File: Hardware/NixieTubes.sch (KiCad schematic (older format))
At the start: 14 parts, among them U1 HV5623K7-G, U2 HV5623K7-G

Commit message: Start rework
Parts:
- N1, N2, N3, N4: footprint Nixies:nixies-us-IN-14 -> Nixies:IN-14
- U1, U2: value HV5623K7-G -> HV5530; footprint hv5623:HV5623K7-G -> Package_QFP:PQFP-44_10x10mm_P0.8mm; symbol 2020-07-19_08-41-54:HV5623K7-G -> HV_Shift_Register:HV5530
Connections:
- wire segments 135 -> 131
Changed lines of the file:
@@
 Wire Wire Line
 	950  3300 1150 3300
-Text GLabel 3500 4100 2    50   Input ~ 0
+Text GLabel 3500 4000 2    50   Input ~ 0
 NIX_LE
-Text GLabel 3500 4000 2    50   Input ~ 0
+Text GLabel 3500 3900 2    50   Input ~ 0
 NIX_DATA
-Text GLabel 3500 4400 2    50   Input ~ 0
+Text GLabel 3500 4300 2    50   Input ~ 0
 NIX_CLK
 Wire Wire Line
-	3350 4400 3500 4400
-Wire Wire Line
-	3350 4100 3500 4100
+	3350 4300 3500 4300
 Wire Wire Line
 	3350 4000 3500 4000
+Wire Wire Line
+	3350 3900 3500 3900
 $Comp
 L power:+5V #PWR0101
 U 1 1 5F1E1656
-P 3500 4200
-F 0 "#PWR0101" H 3500 4050 50  0001 C CNN
-F 1 "+5V" V 3515 4328 50  0000 L CNN
-F 2 "" H 3500 4200 50  0001 C CNN
-F 3 "" H 3500 4200 50  0001 C CNN
-	1    3500 4200
+P 3500 4100
+F 0 "#PWR0101" H 3500 3950 50  0001 C CNN
+F 1 "+5V" V 3515 4228 50  0000 L CNN
+F 2 "" H 3500 4100 50  0001 C CNN
+F 3 "" H 3500 4100 50  0001 C CNN
+	1    3500 4100
 	0    1    1    0
 $EndComp
-Wire Wire Line
-	3500 4200 3350 4200
 $Comp
 L power:+5V #PWR0103
 U 1 1 5F1E5BAE
-P 3500 4500
-F 0 "#PWR0103" H 3500 4350 50  0001 C CNN
-F 1 "+5V" V 3515 4628 50  0000 L CNN
-F 2 "" H 3500 4500 50  0001 C CNN
-F 3 "" H 3500 4500 50  0001 C CNN
-	1    3500 4500
+P 3500 4400
+F 0 "#PWR0103" H 3500 4250 50  0001 C CNN
+F 1 "+5V" V 3515 4528 50  0000 L CNN
+F 2 "" H 3500 4400 50  0001 C CNN
+F 3 "" H 3500 4400 50  0001 C CNN
+	1    3500 4400
 	0    1    1    0
 $EndComp
 Wire Wire Line
-	3350 4500 3500 4500
+	3350 4400 3500 4400
 $Comp
 L power:+5V #PWR0104
@@
 	1    0    0    -1
 $EndComp
-Text GLabel 6850 4100 2    50   Input ~ 0
+Text GLabel 6850 4000 2    50   Input ~ 0
 NIX_LE
-Text GLabel 6850 4400 2    50   Input ~ 0
+Text GLabel 6850 4300 2    50   Input ~ 0
 NIX_CLK
 Wire Wire Line
-	6700 4300 6800 4300
-Wire Wire Line
-	6700 4400 6850 4400
-Wire Wire Line
-	6700 4100 6850 4100
-Wire Wire Line
-	6700 2700 6800 2700
-Wire Wire Line
-	6800 2700 6800 4300
-Connection ~ 6800 4300
+	6700 4200 6800 4200
+Wire Wire Line
+	6700 4300 6850 4300
+Wire Wire Line
+	6700 4000 6850 4000
 $Comp
 L power:+5V #PWR0107
 U 1 1 5F54A366
-P 6850 4200
-F 0 "#PWR0107" H 6850 4050 50  0001 C CNN
-F 1 "+5V" V 6865 4328 50  0000 L CNN
-F 2 "" H 6850 4200 50  0001 C CNN
-F 3 "" H 6850 4200 50  0001 C CNN
-	1    6850 4200
+P 6850 4100
+F 0 "#PWR0107" H 6850 3950 50  0001 C CNN
+F 1 "+5V" V 6865 4228 50  0000 L CNN
+F 2 "" H 6850 4100 50  0001 C CNN
+F 3 "" H 6850 4100 50  0001 C CNN
+	1    6850 4100
 	0    1    1    0
 $EndComp
 Wire Wire Line
-	6850 4200 6700 4200
-Wire Wire Line
-	6700 3900 6850 3900
+	6850 4100 6700 4100
+Wire Wire Line
+	6700 3800 6850 3800
 $Comp
 L power:+5V #PWR0109
 U 1 1 5F54A37C
-P 6850 4500
-F 0 "#PWR0109" H 6850 4350 50  0001 C CNN
-F 1 "+5V" V 6865 4628 50  0000 L CNN
-F 2 "" H 6850 4500 50  0001 C CNN
-F 3 "" H 6850 4500 50  0001 C CNN
-	1    6850 4500
+P 6850 4400
+F 0 "#PWR0109" H 6850 4250 50  0001 C CNN
+F 1 "+5V" V 6865 4528 50  0000 L CNN
+F 2 "" H 6850 4400 50  0001 C CNN
+F 3 "" H 6850 4400 50  0001 C CNN
+	1    6850 4400
 	0    1    1    0
 $EndComp
 Wire Wire Line
-	6800 4300 6800 5000
-Wire Wire Line
-	6700 4500 6850 4500
-Wire Wire Line
-	3350 4900 3750 4900
-Wire Wire Line
-	3750 4900 3750 5400
+	6700 4400 6850 4400
 Wire Wire Line
 	3750 5400 7450 5400
 Wire Wire Line
-	7450 5400 7450 4000
-Wire Wire Line
-	6700 4000 7450 4000
+	6700 3900 7450 3900
 Text Label 1000 3300 0    50   ~ 0
 N1_4
@@
 NoConn ~ 100  3600
 $Comp
-L 2020-07-19_08-41-54:HV5623K7-G U1
+L HV_Shift_Register:HV5530 U1
 U 1 1 5F15D56D
 P 1150 2700
 F 0 "U1" H 2250 3087 60  0000 C CNN
-F 1 "HV5623K7-G" H 2250 2981 60  0000 C CNN
-F 2 "hv5623:HV5623K7-G" H 2250 2940 60  0001 C CNN
+F 1 "HV5530" H 2250 2981 60  0000 C CNN
+F 2 "Package_QFP:PQFP-44_10x10mm_P0.8mm" H 2250 2940 60  0001 C CNN
 F 3 "" H 1150 2700 60  0000 C CNN
 	1    1150 2700
 	1    0    0    -1
 $EndComp
+Text Label 3500 3200 0    50   ~ 0
+N2_9
 Text Label 3500 3300 0    50   ~ 0
-N2_9
-Text Label 3500 3400 0    50   ~ 0
 N2_8
 $Comp
@@
 F 0 "N1" V 1800 1500 45  0000 R CNN
 F 1 "IN-14" H 1450 1300 45  0001 L BNN
-F 2 "Nixies:nixies-us-IN-14" H 1480 1450 20  0001 C CNN
+F 2 "Nixies:IN-14" H 1480 1450 20  0001 C CNN
 F 3 "" H 1450 1300 50  0001 C CNN
 	1    1450 1300
@@
 	2050 900  1850 900
 Text Label 1850 900  0    50   ~ 0
-N1_R
+N1_L
 Wire Wire Line
 	2050 1800 1850 1800
 Text Label 1850 1800 0    50   ~ 0
-N1_L
+N1_R
 Text GLabel 2100 1400 2    50   Input ~ 0
 170V
@@
 F 0 "N2" V 3450 1500 45  0000 R CNN
 F 1 "IN-14" H 3100 1300 45  0001 L BNN
-F 2 "Nixies:nixies-us-IN-14" H 3130 1450 20  0001 C CNN
+F 2 "Nixies:IN-14" H 3130 1450 20  0001 C CNN
 F 3 "" H 3100 1300 50  0001 C CNN
 	1    3100 1300
@@
 	3700 900  3500 900
 Text Label 3500 900  0    50   ~ 0
-N2_R
+N2_L
 Wire Wire Line
 	3700 1800 3500 1800
 Text Label 3500 1800 0    50   ~ 0
-N2_L
+N2_R
 Text GLabel 3750 1400 2    50   Input ~ 0
 170V
@@
 F 0 "N3" V 5100 1500 45  0000 R CNN
 F 1 "IN-14" H 4750 1300 45  0001 L BNN
-F 2 "Nixies:nixies-us-IN-14" H 4780 1450 20  0001 C CNN
+F 2 "Nixies:IN-14" H 4780 1450 20  0001 C CNN
 F 3 "" H 4750 1300 50  0001 C CNN
 	1    4750 1300
@@
 	5350 900  5150 900
 Text Label 5150 900  0    50   ~ 0
-N3_R
+N3_L
 Wire Wire Line
 	5350 1800 5150 1800
 Text Label 5150 1800 0    50   ~ 0
-N3_L
+N3_R
 Text GLabel 5400 1400 2    50   Input ~ 0
 170V
@@
 F 0 "N4" V 6750 1500 45  0000 R CNN
 F 1 "IN-14" H 6400 1300 45  0001 L BNN
-F 2 "Nixies:nixies-us-IN-14" H 6430 1450 20  0001 C CNN
+F 2 "Nixies:IN-14" H 6430 1450 20  0001 C CNN
 F 3 "" H 6400 1300 50  0001 C CNN
 	1    6400 1300
@@
 	7000 900  6800 900
 Text Label 6800 900  0    50   ~ 0
-N4_R
+N4_L
 Wire Wire Line
 	7000 1800 6800 1800
 Text Label 6800 1800 0    50   ~ 0
-N4_L
+N4_R
 Text GLabel 7050 1400 2    50   Input ~ 0
 170V
@@
 Wire Wire Line
 	7000 1400 7050 1400
-Text Label 3700 3200 2    50   ~ 0
+Text Label 3700 3100 2    50   ~ 0
 N2_0
-Text Label 3700 3100 2    50   ~ 0
+Text Label 3700 3000 2    50   ~ 0
 N2_R
-Text Label 3700 3000 2    50   ~ 0
+Text Label 3700 2900 2    50   ~ 0
 N2_L
-Text Label 3700 2900 2    50   ~ 0
+Text Label 3700 2800 2    50   ~ 0
 N2_1
-Text Label 3700 2800 2    50   ~ 0
+Text Label 3700 2700 2    50   ~ 0
 N2_2
 Text Label 1000 2700 0    50   ~ 0
@@
 N2_5
 Wire Wire Line
-	3350 3400 3750 3400
-Wire Wire Line
 	3350 3300 3750 3300
+Wire Wire Line
+	3350 3200 3750 3200
 Wire Wire Line
 	4500 4000 4300 4000
@@
 Text Label 4350 4000 0    50   ~ 0
 N3_R
-Text Label 7050 2800 2    50   ~ 0
+Text Label 7050 2700 2    50   ~ 0
 N4_2
 Text Label 4350 2700 0    50   ~ 0
@@
 Text Label 4350 3100 0    50   ~ 0
 N4_7
-Text Label 7050 3400 2    50   ~ 0
+Text Label 7050 3300 2    50   ~ 0
 N4_8
-Text Label 7050 3300 2    50   ~ 0
+Text Label 7050 3200 2    50   ~ 0
 N4_9
-Text Label 7050 3200 2    50   ~ 0
+Text Label 7050 3100 2    50   ~ 0
 N4_0
-Text Label 7050 3100 2    50   ~ 0
+Text Label 7050 3000 2    50   ~ 0
 N4_R
+Text Label 6850 2800 0    50   ~ 0
+N4_1
 Text Label 6850 2900 0    50   ~ 0
-N4_1
-Text Label 6850 3000 0    50   ~ 0
 N4_L
 Wire Wire Line
-	6700 3000 7100 3000
-Wire Wire Line
 	6700 2900 7100 2900
 Wire Wire Line
+	6700 2800 7100 2800
+Wire Wire Line
 	1150 2900 950  2900
 Wire Wire Line
@@
 	1150 2700 950  2700
 Wire Wire Line
+	3350 2700 3750 2700
+Wire Wire Line
 	3350 2800 3750 2800
 Wire Wire Line
@@
 Wire Wire Line
 	3350 3100 3750 3100
-Wire Wire Line
-	3350 3200 3750 3200
 NoConn ~ 1150 3200
 NoConn ~ 1150 4800
 Wire Wire Line
+	6700 3200 7100 3200
+Wire Wire Line
 	6700 3300 7100 3300
 Wire Wire Line
-	6700 3400 7100 3400
-Wire Wire Line
 	4500 3100 4300 3100
 Wire Wire Line
@@
 	4500 2700 4300 2700
 Wire Wire Line
-	6700 2800 7100 2800
+	6700 2700 7100 2700
 $Comp
 L power:GND #PWR0110
@@
 $EndComp
 Wire Wire Line
-	3450 4300 3450 5000
-Wire Wire Line
-	3350 4300 3450 4300
-NoConn ~ 6700 4900
-Text GLabel 6850 3900 2    50   Input ~ 0
+	3350 4200 3450 4200
+Text GLabel 6850 3800 2    50   Input ~ 0
 NIX_DIM
 Wire Wire Line
-	3350 2700 3450 2700
-Connection ~ 3450 4300
-Wire Wire Line
-	3450 2700 3450 4300
-Wire Wire Line
-	3350 3900 3500 3900
-Text GLabel 3500 3900 2    50   Input ~ 0
+	3350 3800 3500 3800
+Text GLabel 3500 3800 2    50   Input ~ 0
 NIX_DIM
 $Comp
@@
 Wire Wire Line
 	8250 1250 8200 1250
-Text Label 3700 3500 2    50   ~ 0
+Text Label 3700 3400 2    50   ~ 0
 N_DOT
 Wire Wire Line
@@
 N2_7
 NoConn ~ 3350 3600
-NoConn ~ 3350 3700
 NoConn ~ 1150 4600
 NoConn ~ 1150 4700
 $Comp
-L 2020-07-19_08-41-54:HV5623K7-G U2
+L HV_Shift_Register:HV5530 U2
 U 1 1 5F664441
 P 4500 2700
 F 0 "U2" H 5600 3087 60  0000 C CNN
-F 1 "HV5623K7-G" H 5600 2981 60  0000 C CNN
-F 2 "hv5623:HV5623K7-G" H 5600 2940 60  0001 C CNN
+F 1 "HV5530" H 5600 2981 60  0000 C CNN
+F 2 "Package_QFP:PQFP-44_10x10mm_P0.8mm" H 5600 2940 60  0001 C CNN
 F 3 "" H 4500 2700 60  0000 C CNN
 	1    4500 2700
@@
 NoConn ~ 4500 4800
 Wire Wire Line
-	6700 3200 7100 3200
-Wire Wire Line
 	6700 3100 7100 3100
+Wire Wire Line
+	6700 3000 7100 3000
 NoConn ~ 6700 3500
 NoConn ~ 6700 3600
-NoConn ~ 6700 3700
 NoConn ~ 4500 3200
 NoConn ~ 4500 4500
 Wire Wire Line
-	3350 3500 3750 3500
+	3350 3400 3750 3400
 NoConn ~ 1150 4500
+NoConn ~ 3350 3500
+Wire Wire Line
+	3350 4100 3500 4100
+Wire Wire Line
+	3350 4800 3750 4800
+Wire Wire Line
+	3450 4200 3450 5000
+Wire Wire Line
+	3750 4800 3750 5400
+NoConn ~ 6700 3400
+Wire Wire Line
+	7450 3900 7450 5400
+NoConn ~ 6700 4800
+Wire Wire Line
+	6800 4200 6800 5000
 $EndSCHEMATC

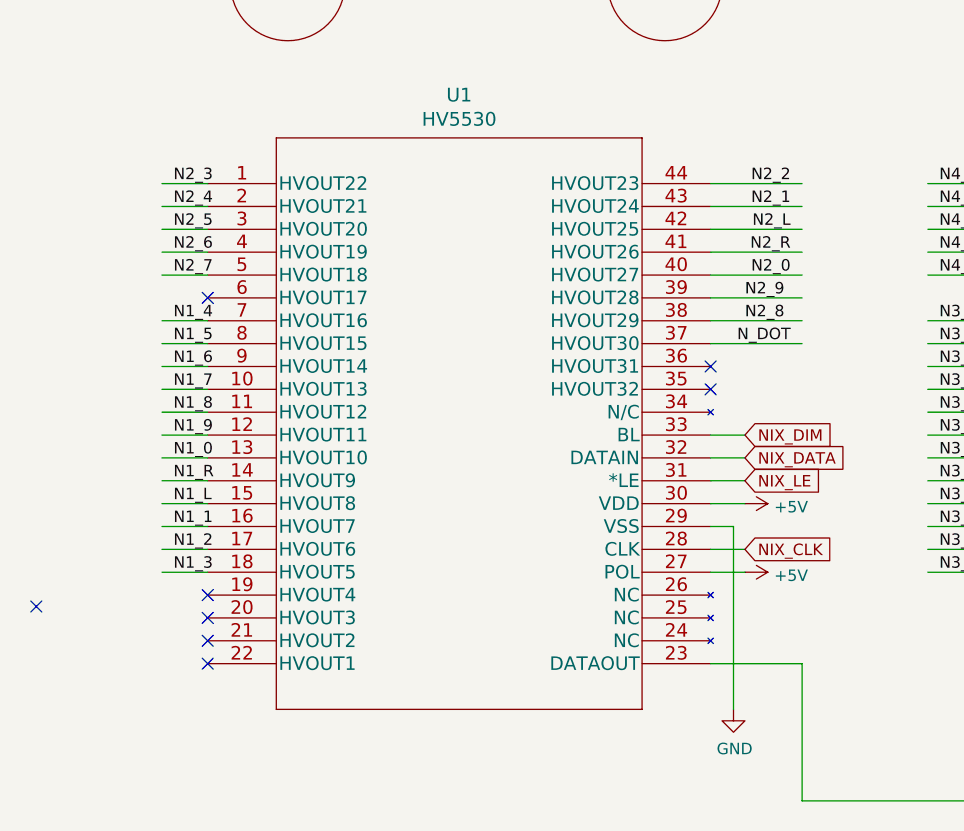
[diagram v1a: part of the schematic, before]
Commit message: Fix packages, route left nixies
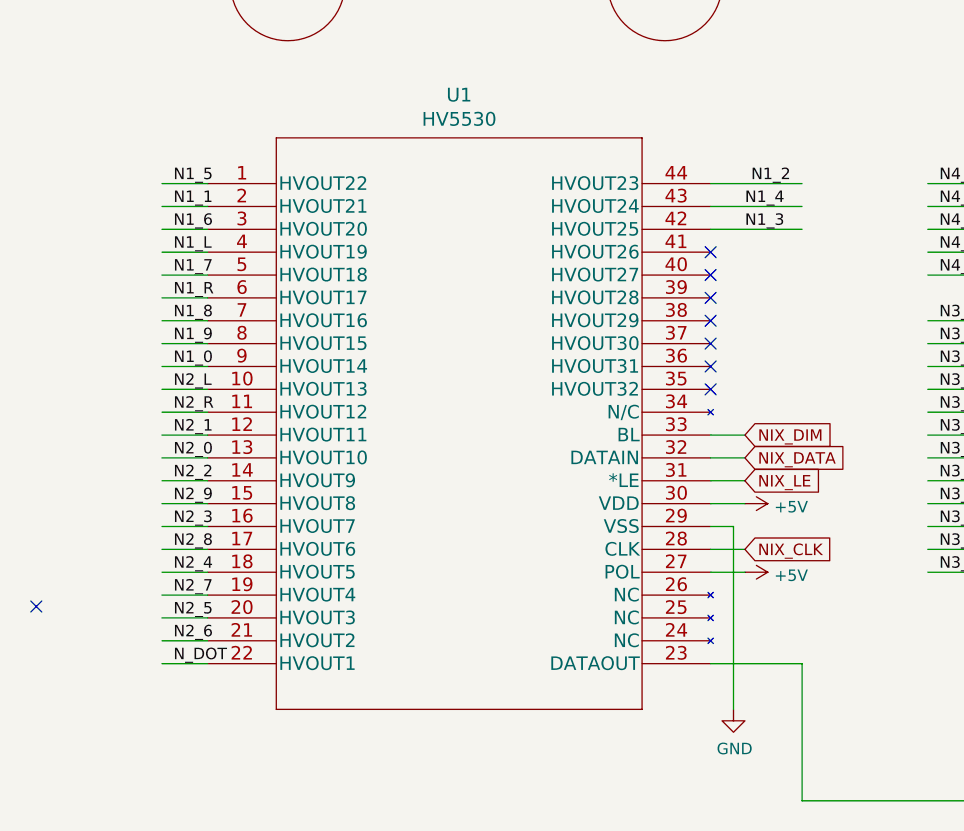
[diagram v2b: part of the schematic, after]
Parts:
- C1, C2: footprint Capacitor_SMD:C_0603_1608Metric_Pad1.05x0.95mm_HandSolder -> Capacitor_SMD:C_0603_1608Metric
- R1, R10, R2, R3, R4: footprint Resistor_SMD:R_1206_3216Metric_Pad1.42x1.75mm_HandSolder -> Resistor_SMD:R_1206_3216Metric
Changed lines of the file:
@@
 Wire Wire Line
 	1150 3600 950  3600
-Wire Wire Line
-	1150 3500 950  3500
-Wire Wire Line
-	1150 3400 950  3400
-Wire Wire Line
-	950  3300 1150 3300
 Text GLabel 3500 4000 2    50   Input ~ 0
 NIX_LE
@@
 F 0 "C1" H 742 7346 50  0000 L CNN
 F 1 "100n" H 742 7255 50  0000 L CNN
-F 2 "Capacitor_SMD:C_0603_1608Metric_Pad1.05x0.95mm_HandSolder" H 650 7300 50  0001 C CNN
+F 2 "Capacitor_SMD:C_0603_1608Metric" H 650 7300 50  0001 C CNN
 F 3 "~" H 650 7300 50  0001 C CNN
 	1    650  7300
@@
 F 0 "C2" H 1142 7346 50  0000 L CNN
 F 1 "100n" H 1142 7255 50  0000 L CNN
-F 2 "Capacitor_SMD:C_0603_1608Metric_Pad1.05x0.95mm_HandSolder" H 1050 7300 50  0001 C CNN
+F 2 "Capacitor_SMD:C_0603_1608Metric" H 1050 7300 50  0001 C CNN
 F 3 "~" H 1050 7300 50  0001 C CNN
 	1    1050 7300
@@
 Wire Wire Line
 	6700 3900 7450 3900
-Text Label 1000 3300 0    50   ~ 0
-N1_4
-Text Label 1000 3400 0    50   ~ 0
-N1_5
-Text Label 1000 3500 0    50   ~ 0
-N1_6
 Text Label 1000 3600 0    50   ~ 0
-N1_7
+N2_L
 Text Label 1000 3700 0    50   ~ 0
-N1_8
+N2_R
 Text Label 1000 3800 0    50   ~ 0
-N1_9
+N2_1
 Text Label 1000 3900 0    50   ~ 0
-N1_0
+N2_0
 Text Label 1000 4000 0    50   ~ 0
-N1_R
+N2_2
 Text Label 1000 4100 0    50   ~ 0
-N1_L
+N2_9
 Text Label 1000 4200 0    50   ~ 0
-N1_1
+N2_3
 Text Label 1000 4300 0    50   ~ 0
-N1_2
+N2_8
 Text Label 1000 4400 0    50   ~ 0
-N1_3
+N2_4
 NoConn ~ 400  4550
 NoConn ~ 100  3600
@@
 	1    0    0    -1
 $EndComp
-Text Label 3500 3200 0    50   ~ 0
-N2_9
-Text Label 3500 3300 0    50   ~ 0
-N2_8
 $Comp
 L nixies-us:IN-14 N1
@@
 F 0 "R1" V 1754 1400 50  0000 C CNN
 F 1 "10k" V 1845 1400 50  0000 C CNN
-F 2 "Resistor_SMD:R_1206_3216Metric_Pad1.42x1.75mm_HandSolder" H 1950 1400 50  0001 C CNN
+F 2 "Resistor_SMD:R_1206_3216Metric" H 1950 1400 50  0001 C CNN
 F 3 "~" H 1950 1400 50  0001 C CNN
 	1    1950 1400
@@
 F 0 "R2" V 3404 1400 50  0000 C CNN
 F 1 "10k" V 3495 1400 50  0000 C CNN
-F 2 "Resistor_SMD:R_1206_3216Metric_Pad1.42x1.75mm_HandSolder" H 3600 1400 50  0001 C CNN
+F 2 "Resistor_SMD:R_1206_3216Metric" H 3600 1400 50  0001 C CNN
 F 3 "~" H 3600 1400 50  0001 C CNN
 	1    3600 1400
@@
 F 0 "R3" V 5054 1400 50  0000 C CNN
 F 1 "10k" V 5145 1400 50  0000 C CNN
-F 2 "Resistor_SMD:R_1206_3216Metric_Pad1.42x1.75mm_HandSolder" H 5250 1400 50  0001 C CNN
+F 2 "Resistor_SMD:R_1206_3216Metric" H 5250 1400 50  0001 C CNN
 F 3 "~" H 5250 1400 50  0001 C CNN
 	1    5250 1400
@@
 F 0 "R4" V 6704 1400 50  0000 C CNN
 F 1 "10k" V 6795 1400 50  0000 C CNN
-F 2 "Resistor_SMD:R_1206_3216Metric_Pad1.42x1.75mm_HandSolder" H 6900 1400 50  0001 C CNN
+F 2 "Resistor_SMD:R_1206_3216Metric" H 6900 1400 50  0001 C CNN
 F 3 "~" H 6900 1400 50  0001 C CNN
 	1    6900 1400
@@
 Wire Wire Line
 	7000 1400 7050 1400
-Text Label 3700 3100 2    50   ~ 0
-N2_0
-Text Label 3700 3000 2    50   ~ 0
-N2_R
-Text Label 3700 2900 2    50   ~ 0
-N2_L
-Text Label 3700 2800 2    50   ~ 0
-N2_1
-Text Label 3700 2700 2    50   ~ 0
-N2_2
-Text Label 1000 2700 0    50   ~ 0
-N2_3
-Text Label 1000 2800 0    50   ~ 0
-N2_4
-Text Label 1000 2900 0    50   ~ 0
-N2_5
-Wire Wire Line
-	3350 3300 3750 3300
-Wire Wire Line
-	3350 3200 3750 3200
 Wire Wire Line
 	4500 4000 4300 4000
@@
 	6700 2800 7100 2800
 Wire Wire Line
-	1150 2900 950  2900
-Wire Wire Line
-	1150 2800 950  2800
-Wire Wire Line
-	1150 2700 950  2700
-Wire Wire Line
-	3350 2700 3750 2700
-Wire Wire Line
-	3350 2800 3750 2800
-Wire Wire Line
-	3350 2900 3750 2900
-Wire Wire Line
-	3350 3000 3750 3000
-Wire Wire Line
-	3350 3100 3750 3100
-NoConn ~ 1150 3200
-NoConn ~ 1150 4800
-Wire Wire Line
 	6700 3200 7100 3200
 Wire Wire Line
@@
 F 0 "R10" V 8154 1250 50  0000 C CNN
 F 1 "100k" V 8245 1250 50  0000 C CNN
-F 2 "Resistor_SMD:R_1206_3216Metric_Pad1.42x1.75mm_HandSolder" H 8350 1250 50  0001 C CNN
+F 2 "Resistor_SMD:R_1206_3216Metric" H 8350 1250 50  0001 C CNN
 F 3 "~" H 8350 1250 50  0001 C CNN
 	1    8350 1250
@@
 Wire Wire Line
 	8250 1250 8200 1250
-Text Label 3700 3400 2    50   ~ 0
-N_DOT
-Wire Wire Line
-	1150 3100 950  3100
-Wire Wire Line
-	1150 3000 950  3000
-Text Label 1000 3000 0    50   ~ 0
-N2_6
-Text Label 1000 3100 0    50   ~ 0
-N2_7
-NoConn ~ 3350 3600
-NoConn ~ 1150 4600
-NoConn ~ 1150 4700
 $Comp
 L HV_Shift_Register:HV5530 U2
@@
 NoConn ~ 4500 4500
 Wire Wire Line
-	3350 3400 3750 3400
-NoConn ~ 1150 4500
-NoConn ~ 3350 3500
-Wire Wire Line
 	3350 4100 3500 4100
 Wire Wire Line
@@
 Wire Wire Line
 	6800 4200 6800 5000
+Wire Wire Line
+	1150 4500 950  4500
+Text Label 1000 4500 0    50   ~ 0
+N2_7
+Wire Wire Line
+	1150 4600 950  4600
+Text Label 1000 4600 0    50   ~ 0
+N2_5
+Wire Wire Line
+	1150 4700 950  4700
+Text Label 1000 4700 0    50   ~ 0
+N2_6
+Wire Wire Line
+	1150 4800 950  4800
+Text Label 1000 4800 0    50   ~ 0
+N_DOT
+Wire Wire Line
+	1150 3500 950  3500
+Wire Wire Line
+	1150 3400 950  3400
+Text Label 1000 3000 0    50   ~ 0
+N1_L
+Text Label 1000 3100 0    50   ~ 0
+N1_7
+Text Label 1000 3200 0    50   ~ 0
+N1_R
+Text Label 1000 3300 0    50   ~ 0
+N1_8
+Text Label 1000 3400 0    50   ~ 0
+N1_9
+Text Label 1000 3500 0    50   ~ 0
+N1_0
+Wire Wire Line
+	1150 3300 950  3300
+Wire Wire Line
+	1150 3200 950  3200
+Wire Wire Line
+	1150 3100 950  3100
+Wire Wire Line
+	1150 3000 950  3000
+Text Label 1000 2700 0    50   ~ 0
+N1_5
+Text Label 1000 2800 0    50   ~ 0
+N1_1
+Text Label 1000 2900 0    50   ~ 0
+N1_6
+Wire Wire Line
+	1150 2900 950  2900
+Wire Wire Line
+	1150 2800 950  2800
+Wire Wire Line
+	1150 2700 950  2700
+Text Label 3700 2700 2    50   ~ 0
+N1_2
+Text Label 3500 2800 0    50   ~ 0
+N1_4
+Text Label 3500 2900 0    50   ~ 0
+N1_3
+Wire Wire Line
+	3350 2900 3750 2900
+Wire Wire Line
+	3350 2800 3750 2800
+Wire Wire Line
+	3350 2700 3750 2700
+NoConn ~ 3350 3000
+NoConn ~ 3350 3100
+NoConn ~ 3350 3200
+NoConn ~ 3350 3300
+NoConn ~ 3350 3400
+NoConn ~ 3350 3500
+NoConn ~ 3350 3600
 $EndSCHEMATC

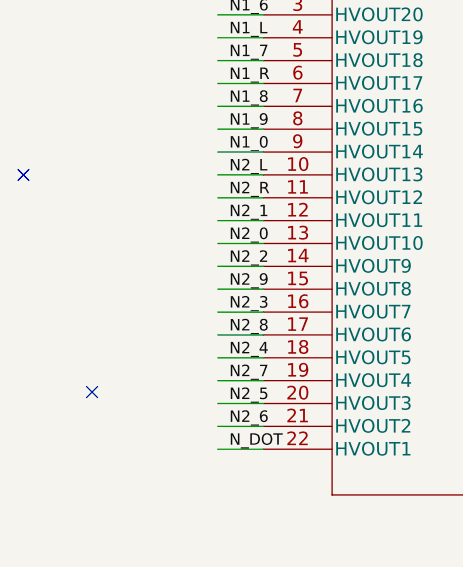
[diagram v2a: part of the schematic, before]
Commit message: Replace LDO
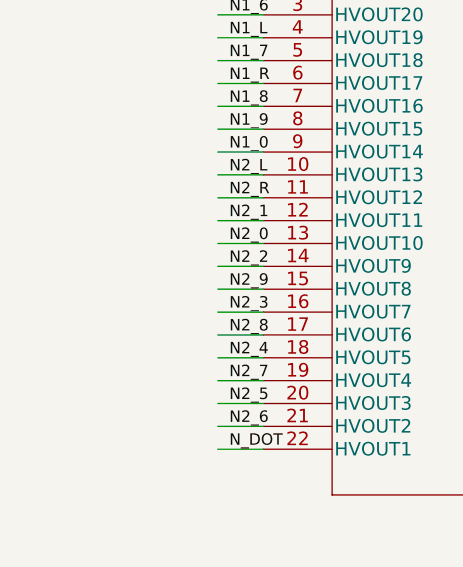
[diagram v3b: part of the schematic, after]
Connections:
- no-connect marks 18 -> 16
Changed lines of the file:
@@
 Text Label 1000 4400 0    50   ~ 0
 N2_4
-NoConn ~ 400  4550
-NoConn ~ 100  3600
 $Comp
 L HV_Shift_Register:HV5530 U1
